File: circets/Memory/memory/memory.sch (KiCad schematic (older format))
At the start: 26 parts

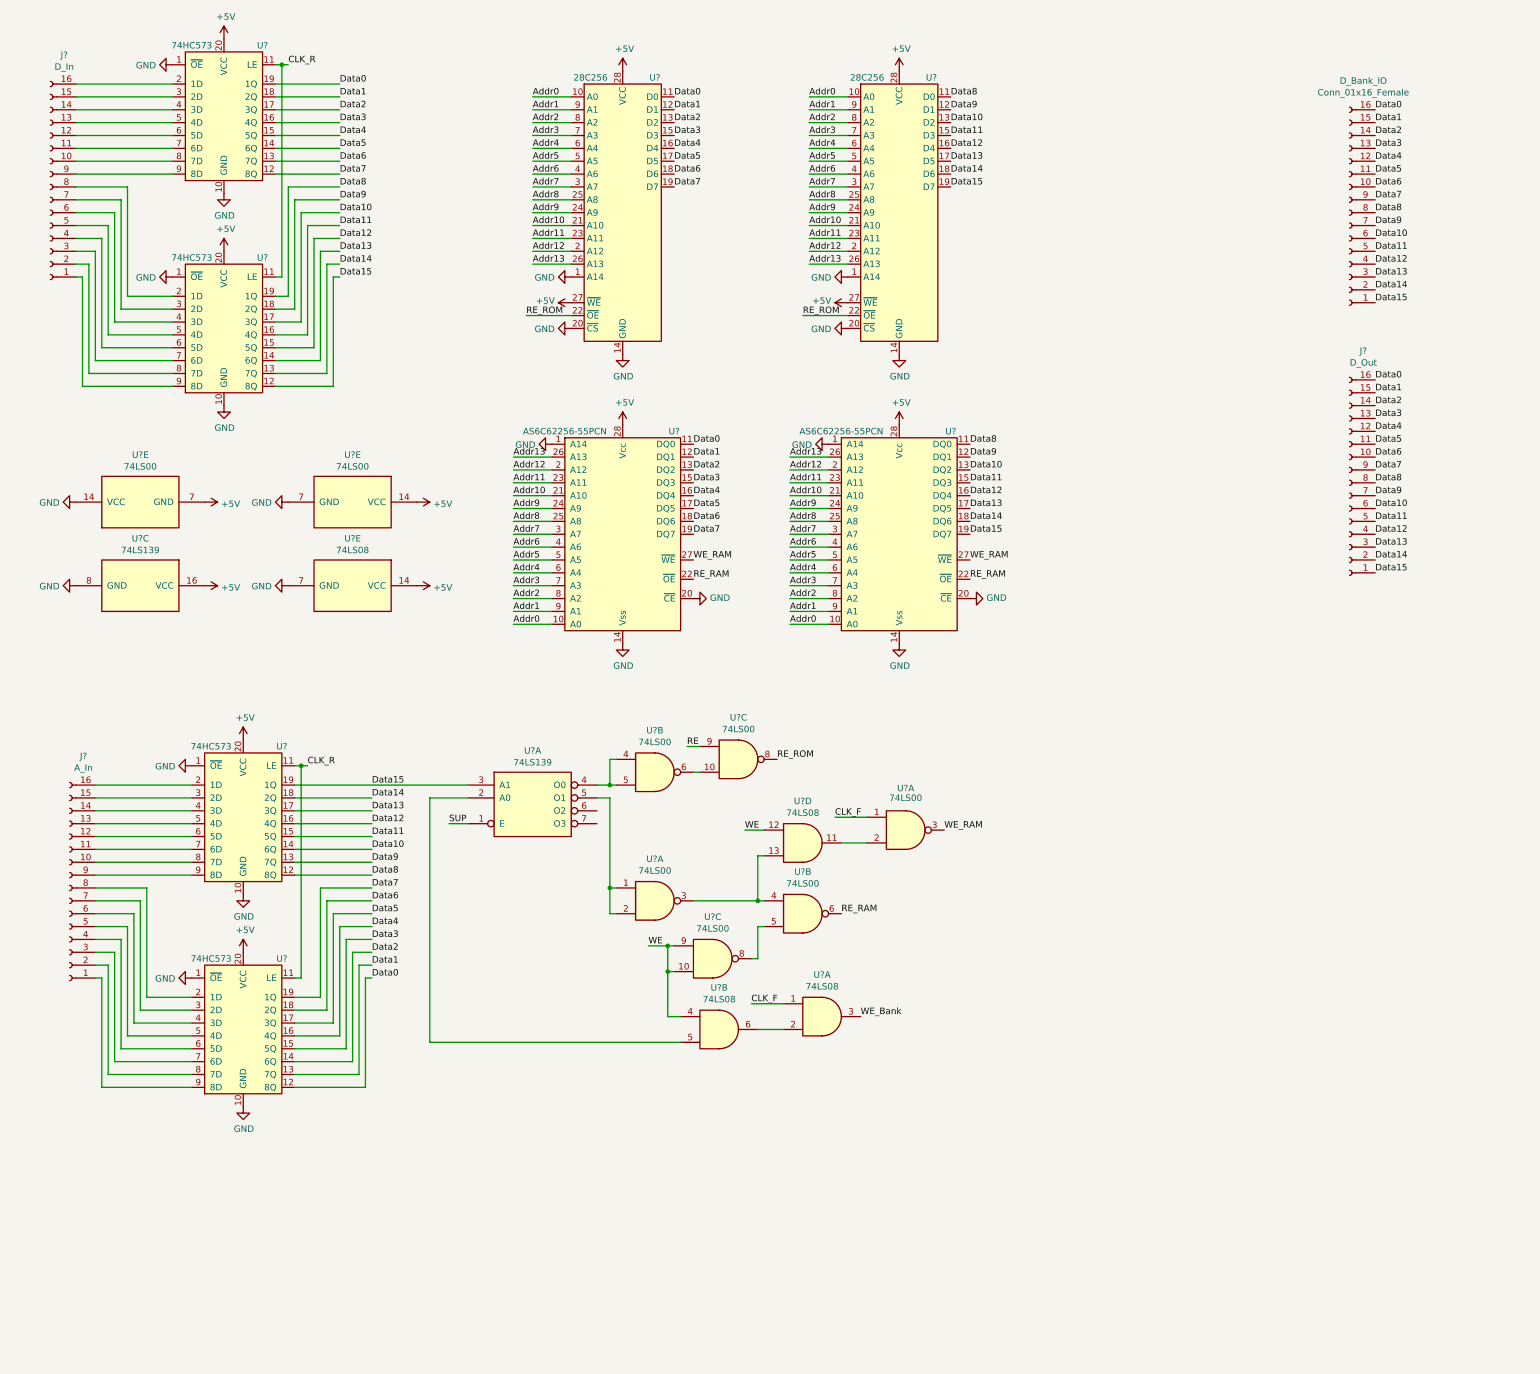
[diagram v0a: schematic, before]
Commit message: Fixed alot of Issues in Memory Module
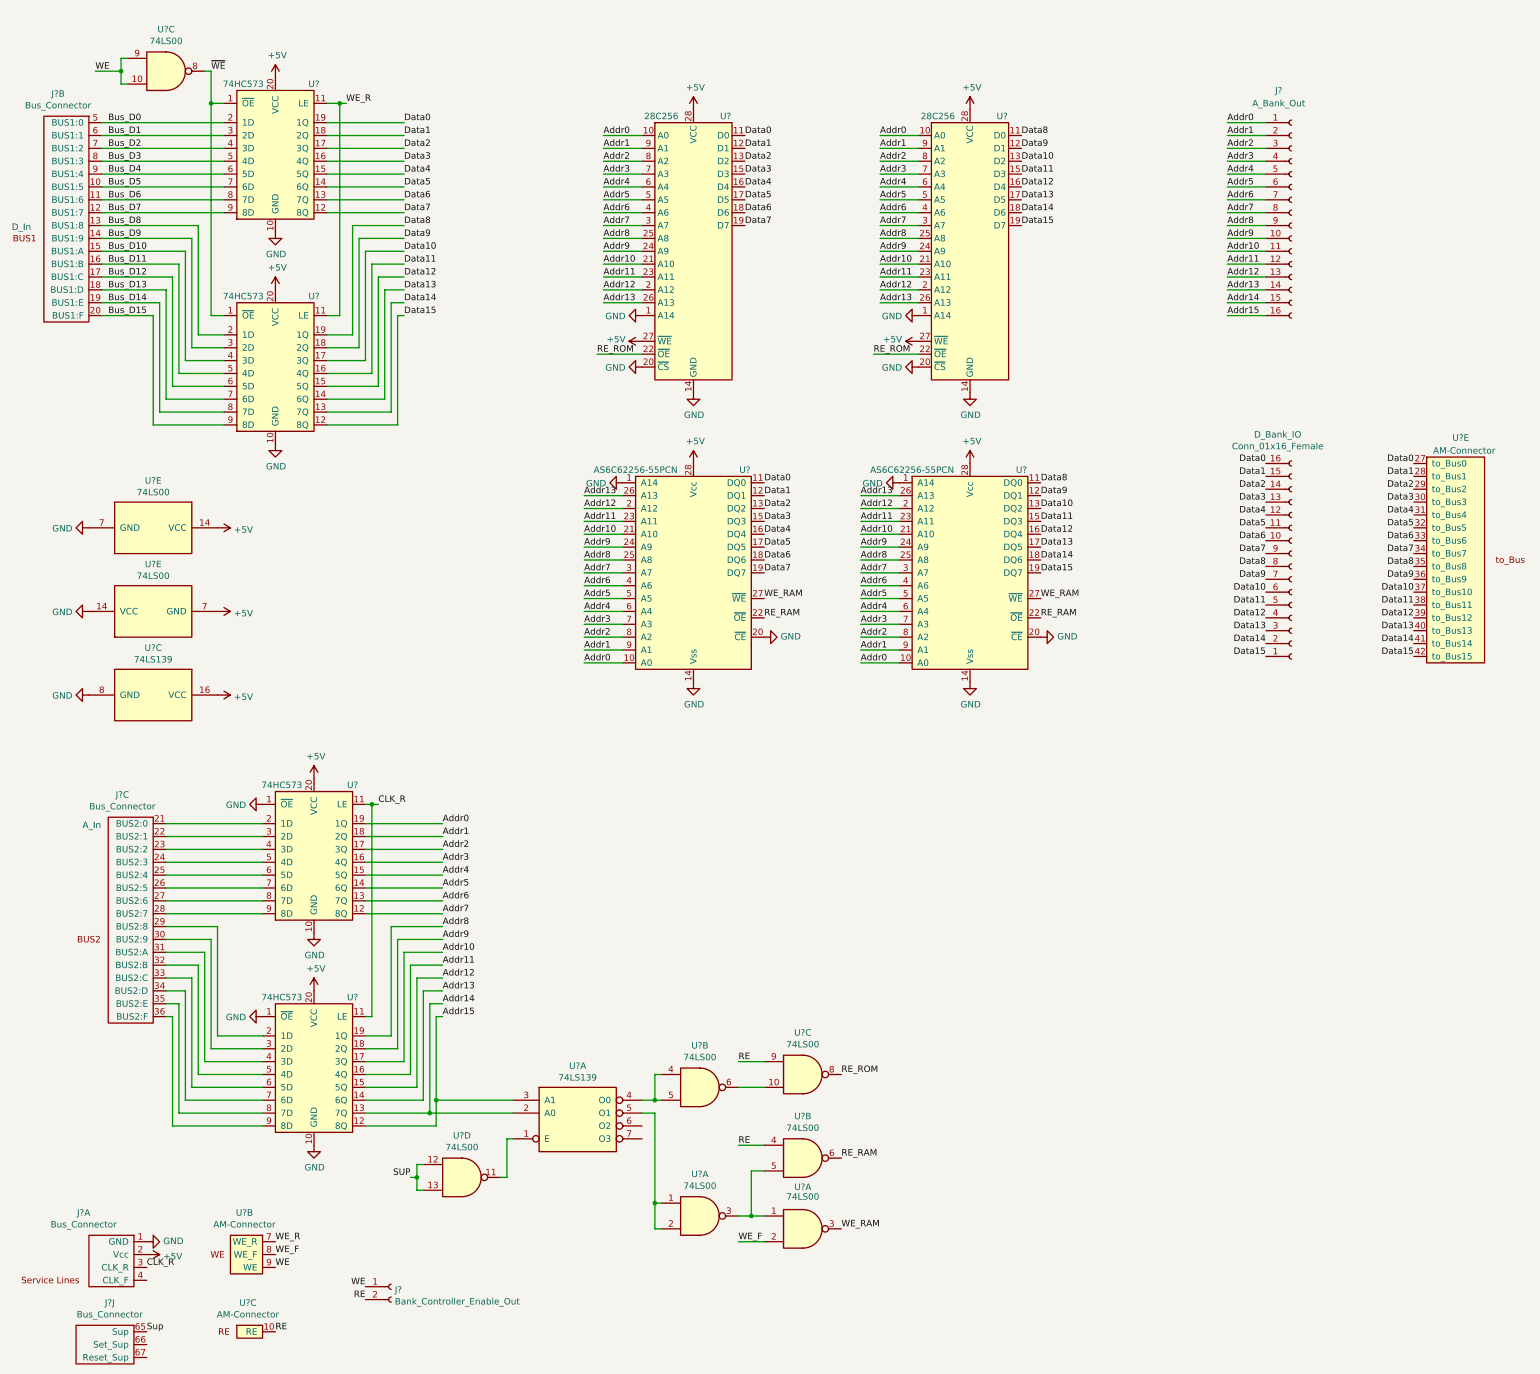
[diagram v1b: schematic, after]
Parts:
- removed J?: D_In, symbol Connector:Conn_01x16_Female
- removed J?: A_In, symbol Connector:Conn_01x16_Female
- removed U? (x4): 74LS08, symbol 74xx:74LS08
- added J? (x4): Bus_Connector, symbol Computer_Component_Library:Bus_Connector
- added J?: Bank_Controller_Enable_Out, symbol Connector:Conn_01x02_Female
- added U? (x3): AM-Connector, symbol Computer_Component_Library:AM-Connector
- added U?: 74LS00, symbol 74xx:74LS00
- J?: value D_Out -> A_Bank_Out
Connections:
- net CLK_F is gone; now on an unnamed net: U?.1
- net +5V: now also J?.2 (Vcc)
- net Addr0: now also J?.1 (Pin_1), U?.19 (1Q)
- net Addr1: now also J?.2 (Pin_2), U?.18 (2Q)
- net Addr10: now also J?.11 (Pin_11), U?.17 (3Q)
- net Addr11: now also J?.12 (Pin_12), U?.16 (4Q)
- net Addr12: now also J?.13 (Pin_13), U?.15 (5Q)
- net Addr13: now also J?.14 (Pin_14), U?.14 (6Q)
- net Addr2: now also J?.3 (Pin_3), U?.17 (3Q)
- net Addr3: now also J?.4 (Pin_4), U?.16 (4Q)
- net Addr4: now also J?.5 (Pin_5), U?.15 (5Q)
- net Addr5: now also J?.6 (Pin_6), U?.14 (6Q)
- net Addr6: now also J?.7 (Pin_7), U?.13 (7Q)
- net Addr7: now also J?.8 (Pin_8), U?.12 (8Q)
- net Addr8: now also J?.9 (Pin_9), U?.19 (1Q)
- net Addr9: now also J?.10 (Pin_10), U?.18 (2Q)
- net CLK_R: now also J?.3 (CLK_R); no longer U?.11 (LE), U?.11 (LE)
- net Data0: now also U?.27 (to_Bus0); no longer J?.16 (Pin_16), U?.12 (8Q)
- net Data1: now also U?.28 (to_Bus1); no longer J?.15 (Pin_15), U?.13 (7Q)
- net Data10: now also U?.37 (to_Bus10); no longer J?.6 (Pin_6), U?.14 (6Q)
- net Data11: now also U?.38 (to_Bus11); no longer J?.5 (Pin_5), U?.15 (5Q)
- net Data12: now also U?.39 (to_Bus12); no longer J?.4 (Pin_4), U?.16 (4Q)
- net Data13: now also U?.40 (to_Bus13); no longer J?.3 (Pin_3), U?.17 (3Q)
- net Data14: now also U?.41 (to_Bus14); no longer J?.2 (Pin_2), U?.18 (2Q)
- net Data15: now also U?.42 (to_Bus15); no longer J?.1 (Pin_1), U?.19 (1Q), U?.3 (A1)
- net Data2: now also U?.29 (to_Bus2); no longer J?.14 (Pin_14), U?.14 (6Q)
- net Data3: now also U?.30 (to_Bus3); no longer J?.13 (Pin_13), U?.15 (5Q)
- net Data4: now also U?.31 (to_Bus4); no longer J?.12 (Pin_12), U?.16 (4Q)
- net Data5: now also U?.32 (to_Bus5); no longer J?.11 (Pin_11), U?.17 (3Q)
- net Data6: now also U?.33 (to_Bus6); no longer J?.10 (Pin_10), U?.18 (2Q)
- net Data7: now also U?.34 (to_Bus7); no longer J?.9 (Pin_9), U?.19 (1Q)
- net Data8: now also U?.35 (to_Bus8); no longer J?.8 (Pin_8), U?.12 (8Q)
- net Data9: now also U?.36 (to_Bus9); no longer J?.7 (Pin_7), U?.13 (7Q)
- net GND: now also J?.1 (GND); no longer U?.1 (~OE), U?.1 (~OE)
- net RE: now also U?.4, J?.2 (Pin_2), U?.10 (RE)
- net SUP: now also U?.12, U?.13; no longer U?.1 (E)
- net WE: now also J?.1 (Pin_1), U?.9 (WE)
- net Bus_D15: now reaches U?.9 (8D)
- net Bus_D15: now also J?.20 (BUS1:F)
- net Bus_D6: now reaches U?.8 (7D)
- net Bus_D6: now also J?.11 (BUS1:6)
- net Bus_D5: now reaches U?.7 (6D)
- net Bus_D5: now also J?.10 (BUS1:5)
- net Bus_D4: now reaches U?.6 (5D)
- net Bus_D4: now also J?.9 (BUS1:4)
- net Bus_D3: now reaches U?.5 (4D)
- net Bus_D3: now also J?.8 (BUS1:3)
- net Bus_D2: now reaches U?.4 (3D)
- net Bus_D2: now also J?.7 (BUS1:2)
- net Bus_D1: now reaches U?.3 (2D)
- net Bus_D1: now also J?.6 (BUS1:1)
- net Bus_D0: now reaches U?.2 (1D)
- net Bus_D0: now also J?.5 (BUS1:0)
- net Bus_D14: now reaches U?.8 (7D)
- net Bus_D14: now also J?.19 (BUS1:E)
- net Bus_D13: now reaches U?.7 (6D)
- net Bus_D13: now also J?.18 (BUS1:D)
- net Bus_D12: now reaches U?.6 (5D)
- net Bus_D12: now also J?.17 (BUS1:C)
- net Bus_D11: now reaches U?.5 (4D)
- net Bus_D11: now also J?.16 (BUS1:B)
- net Bus_D10: now reaches U?.4 (3D)
- net Bus_D10: now also J?.15 (BUS1:A)
- net Bus_D9: now reaches U?.3 (2D)
- net Bus_D9: now also J?.14 (BUS1:9)
- net Bus_D8: now reaches U?.2 (1D)
- net Bus_D8: now also J?.13 (BUS1:8)
- net Bus_D7: now reaches U?.9 (8D)
- net Bus_D7: now also J?.12 (BUS1:7)
- net at U?.9 (8D): now also J?.36 (BUS2:F)
- net at U?.8 (7D): now also J?.27 (BUS2:6)
- net at U?.7 (6D): now also J?.26 (BUS2:5)
- net at U?.6 (5D): now also J?.25 (BUS2:4)
- net at U?.5 (4D): now also J?.24 (BUS2:3)
- net at U?.4 (3D): now also J?.23 (BUS2:2)
- net at U?.3 (2D): now also J?.22 (BUS2:1)
- net at U?.2 (1D): now also J?.21 (BUS2:0)
- net at U?.8 (7D): now also J?.35 (BUS2:E)
- net at U?.7 (6D): now also J?.34 (BUS2:D)
- net at U?.6 (5D): now also J?.33 (BUS2:C)
- net at U?.5 (4D): now also J?.32 (BUS2:B)
- net at U?.4 (3D): now also J?.31 (BUS2:A)
- net at U?.3 (2D): now also J?.30 (BUS2:9)
- net at U?.2 (1D): now also J?.29 (BUS2:8)
- net at U?.9 (8D): now also J?.28 (BUS2:7)
- net Addr14: now reaches U?.2 (A0)
- net Addr14: now also J?.15 (Pin_15), U?.13 (7Q)
- net at U?.3: now also U?.5; no longer U?.4
- net ~WE: now reaches U?.8
- net ~WE: now also U?.1 (~OE), U?.1 (~OE); no longer U?.5
- net WE_F: now reaches U?.2
- net WE_F: now also U?.8 (WE_F)
- new net: U?.1 (E), U?.11
- new net Addr15: J?.16 (Pin_16), U?.12 (8Q), U?.3 (A1)
- new net Sup: J?.65 (Sup)
- new net WE_R: U?.11 (LE), U?.11 (LE), U?.7 (WE_R)
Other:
- note added: "A_In"
- note added: "D_In"
- moved on the sheet: D_Bank_IO, J?, U?, U?A, U?B, U?C, U?E

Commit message: Removed BID Register to Replace with Dual Register
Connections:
- net CLK_R: now also U?.11 (LE), U?.11 (LE)
- removed net WE_R: U?.11 (LE), U?.11 (LE), U?.7 (WE_R)
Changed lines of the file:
@@
 Text Label 2600 10250 0    50   ~ 0
 WE
-Text Label 2600 10050 0    50   ~ 0
-WE_R
 $Comp
 L Computer_Component_Library:AM-Connector U?
@@
 	3100 1200 3150 1200
 Connection ~ 3100 1200
-Text Label 3150 1200 0    50   ~ 0
-WE_R
 Wire Wire Line
 	2100 1200 2200 1200
@@
 Wire Wire Line
 	3700 9550 3700 9650
+Text Label 3150 1200 0    50   ~ 0
+CLK_R
 $EndSCHEMATC
